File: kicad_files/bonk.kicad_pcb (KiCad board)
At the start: 2 copper layers, 246.5 x 75.1 mm, 131 parts, among them J1 Conn_01x04, J2 Conn_01x02, J3 Conn_01x04, J4 USB_C_Receptacle_USB2.0_14P, SW1 SW_Push, U1 XC6206PxxxMR, U2 STM32F072CBTx, U3 USBLC6-2SC6

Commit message: rev01a
added mousebites near usb connector to make removal easier (this is a destructive operation!)

repositioned usb components to reduce number of vias and add space for mousebites
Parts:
- added ?: , , F.Cu at (231.0, 21.2)
- added ?: , , F.Cu at (229.9, 21.2)
- added ?: , , F.Cu at (238.6, 21.2)
- added ?: , , F.Cu at (232.0, 21.2)
- added ?: , , F.Cu at (239.5, 20.7)
- added ?: , , F.Cu at (229.0, 20.7)
- moved F1 1.44 mm to (237.6, 25.5)
- moved R2 0.70 mm to (230.9, 22.9), turned to 180 degrees
- moved R3 0.70 mm to (237.6, 22.9), turned to 180 degrees
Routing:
- net GND: track 35.8 -> 33.2 mm, vias 9 -> 7
- net +5V: track 70.7 -> 69.1 mm, vias 6 -> 0
- net Net-(F1-Pad1): track 13.7 -> 12.5 mm
- net Net-(J4-D--PadA7): track 8.23 -> 7.73 mm
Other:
- board size 246.5 x 75.1 mm -> 246.5 x 75 mm

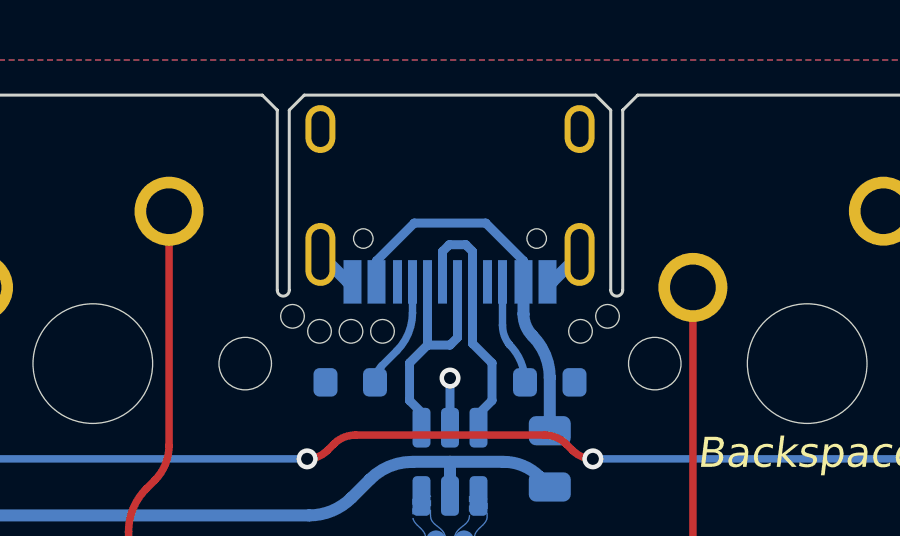
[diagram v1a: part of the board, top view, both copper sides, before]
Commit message: Change USB Connector
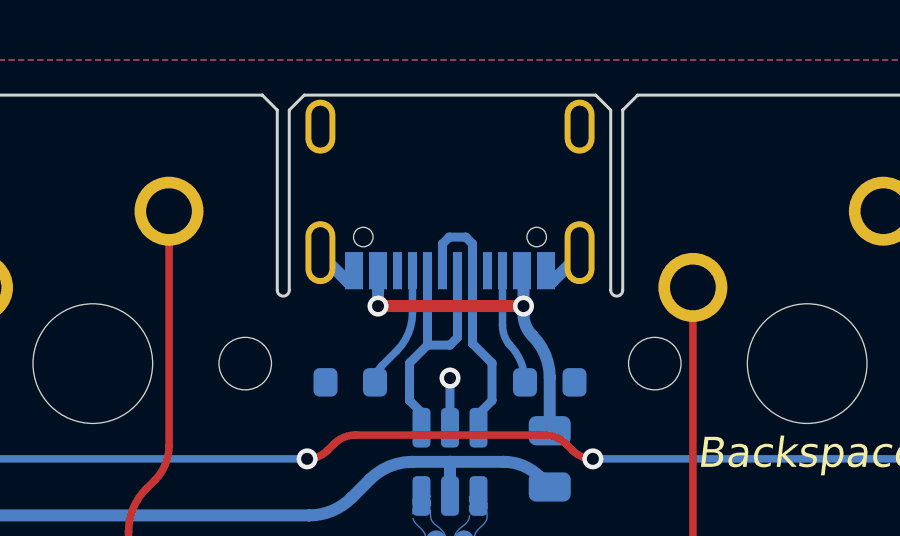
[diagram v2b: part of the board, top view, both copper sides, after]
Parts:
- removed ? (x6): , 
- J4: footprint Connector_USB:USB_C_Receptacle_HRO_TYPE-C-31-M-12 -> Connector_USB:USB_C_Receptacle_G-Switch_GT-USB-7010ASV
- moved J4 0.06 mm to (234.3, 15.5)
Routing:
- net Net-(F1-Pad1): track 12.5 -> 13.0 mm, vias 0 -> 2

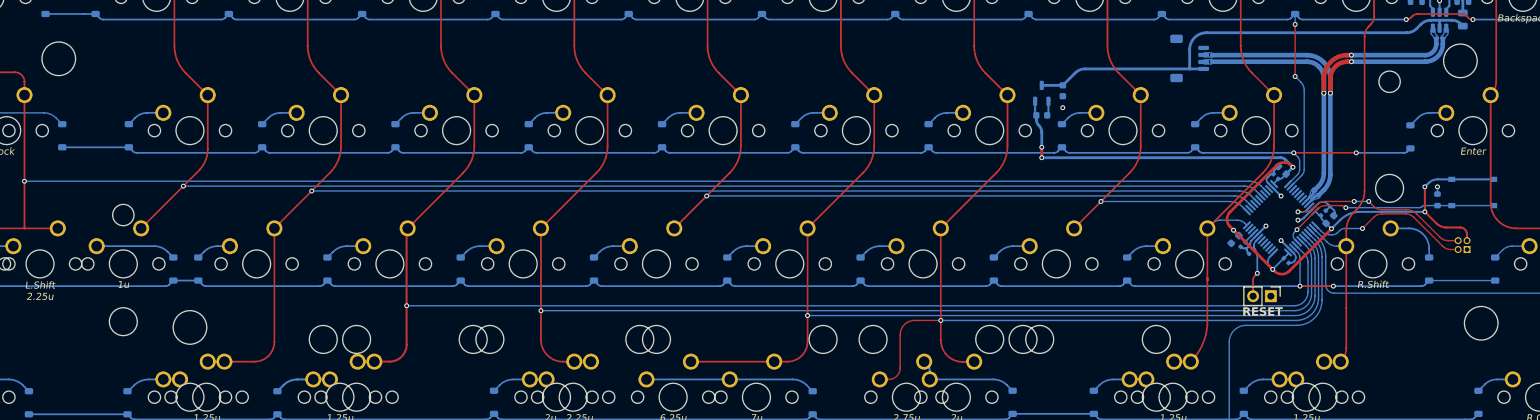
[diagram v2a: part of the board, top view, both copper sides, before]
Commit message: rev1.1
1. Changed reset/boot circuitry to have single-button Reset/Boot functionality.
2. Removed mounting holes
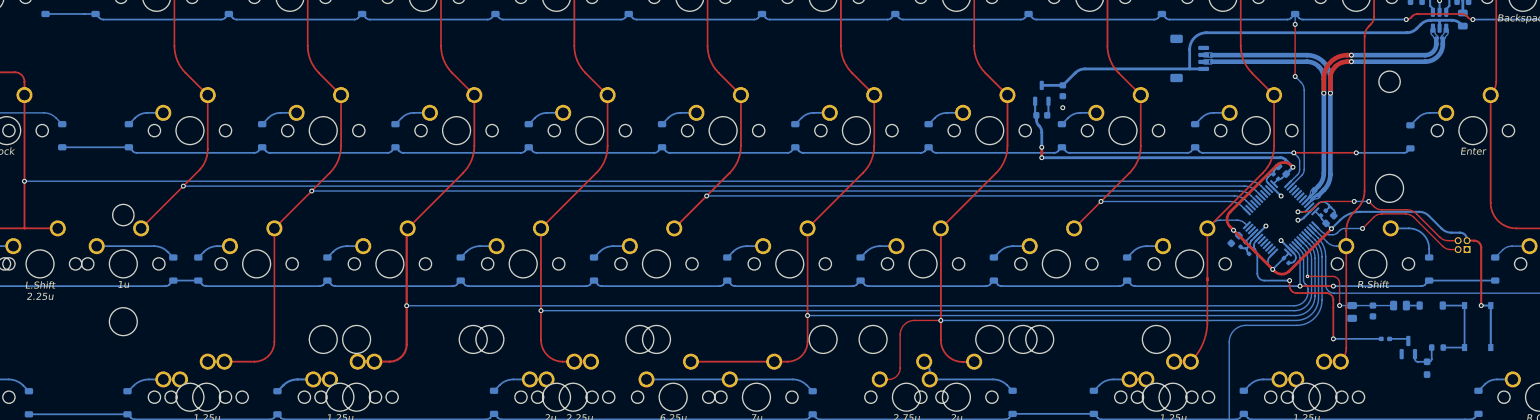
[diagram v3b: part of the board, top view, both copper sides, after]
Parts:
- removed H1, H2, H3, H4: MountingHole, MountingHole:MountingHole_3.2mm_M3
- removed J2: Conn_01x02, Connector_PinHeader_2.54mm:PinHeader_1x02_P2.54mm_Vertical
- added C11: 10u, Capacitor_SMD:C_0603_1608Metric, B.Cu at (224.7, 67.2)
- added D45: 1N4148W, Diode_SMD:D_SOD-123, B.Cu at (233.1, 66.4)
- added Q1: 2N7002, Package_TO_SOT_SMD:SOT-23, B.Cu at (229.8, 72.4)
- added R3: 330k, Resistor_SMD:R_0805_2012Metric, B.Cu at (228.6, 66.4)
- added R5: 100, Resistor_SMD:R_0402_1005Metric_Pad0.72x0.64mm_HandSolder, B.Cu at (226.5, 71.1)
- added R6: 10k, Resistor_SMD:R_0603_1608Metric_Pad0.98x0.95mm_HandSolder, B.Cu at (232.5, 75.3)
- added R7: 1k, Resistor_SMD:R_0603_1608Metric, B.Cu at (234.0, 72.4)
- R4: renamed from R1; value 10k -> 1M; footprint Resistor_SMD:R_0603_1608Metric -> Resistor_SMD:R_0805_2012Metric
- moved R4 20.1 mm to (221.8, 67.3)
- moved SW1 19.2 mm to (239.7, 69.4), turned to -90 degrees
- renumbered R2 to R1, R3 to R2
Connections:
- net Net-(J2-Pin_2) renamed nRST
- R4 pad 1: BOOT -> GND
- R4 pad 2: GND -> BOOT
- SW1 pad 1: BOOT -> Net-(D45-A)
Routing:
- net nRST: track 8.98 -> 31.2 mm, vias 1 -> 2
- net Net-(D45-A): track 0.00 -> 12.2 mm
- net BOOT: track 31.9 -> 22.8 mm
- net Net-(Q1-G): track 0.00 -> 5.15 mm
- net +3V3: track 131.6 -> 135.5 mm, vias 8 -> 7
- net Net-(Q1-D): track 0.00 -> 2.98 mm
- net Net-(D45-K): track 0.00 -> 1.90 mm
- net GND: track 33.2 -> 32.2 mm, vias 7 -> 6
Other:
- board text removed: "BEEP BOOP"
- board text removed: "BOOT"
- board text removed: "RESET"
- board text removed: "you were too strong"
